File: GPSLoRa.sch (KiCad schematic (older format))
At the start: 31 parts, among them P1 IN EXT, P2 - INPUT 12 +, P3 OUT EXT, P4 Battery, Q1 Q_NPN_BCE, U1 4N26, U2 LM2596_Breakout, U3 4N26, U4 RFM95W-868S2, U5 MCP73831T-2ATI/OT

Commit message: ChangeName LoRaCatTrack
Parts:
- A1: footprint (none) -> TIH:GSG-SMA-EDGE
- C1, C2, C3, D1: footprint (none) -> Capacitors_SMD:C_0805_HandSoldering
- D2: footprint (none) -> Diodes_ThroughHole:Diode_TO-220_Horizontal_LargePads
- D3: footprint (none) -> Diodes_ThroughHole:Diode_DO-41_SOD81_Horizontal_RM10
- D4, D5: footprint (none) -> LEDs:LED_0805
- MODULE1: footprint QUECTEL_L80-M39 -> TIH:QUECTEL_L80-M39
- P1, P3: footprint (none) -> Pin_Headers:Pin_Header_Straight_1x01
- P2, P4: footprint (none) -> Pin_Headers:Pin_Header_Straight_1x02
- R1, R2, R3, R4, R5, R6, R7, R8, R9: footprint (none) -> Resistors_SMD:R_0805_HandSoldering
- U1, U3: footprint DIP-6 -> Housings_DIP:DIP-6_W7.62mm_LongPads
- U4: footprint XCVR_RFM95W-868S2 -> TIH:XCVR_RFM95W-868S2
- U5: footprint SOT95P300X145-5N -> TO_SOT_Packages_SMD:SOT-23-5

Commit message: Added PCB
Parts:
- added D6: POWER, LEDs:LED_0805, symbol LED
- added R10: R, Resistors_SMD:R_0805_HandSoldering, symbol R
- D1: footprint Capacitors_SMD:C_0805_HandSoldering -> Diodes_ThroughHole:Diode_DO-35_SOD27_Horizontal_RM10
- D2: footprint Diodes_ThroughHole:Diode_TO-220_Horizontal_LargePads -> Diodes_ThroughHole:Diode_DO-35_SOD27_Horizontal_RM10
- D3: footprint Diodes_ThroughHole:Diode_DO-41_SOD81_Horizontal_RM10 -> Diodes_ThroughHole:Diode_DO-35_SOD27_Horizontal_RM10
- JP1: footprint (none) -> Pin_Headers:Pin_Header_Straight_1x02
- Q1: footprint (none) -> TO_SOT_Packages_THT:TO-92_Inline_Narrow_Oval
- U2: footprint (none) -> TIH:LM2596DC-DC
- uP1: footprint (none) -> TIH:arduinoMiniPro2
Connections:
- net +BATT: now also R10.1
- net GND: now also D6.1 (K)
- new net: D6.2 (A), R10.2
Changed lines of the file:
@@
 F 0 "uP1" H 2350 -250 60  0000 C CNN
 F 1 "ARDUPROMINI" H 1800 -200 60  0000 C CNN
-F 2 "" H 2850 650 60  0001 C CNN
+F 2 "TIH:arduinoMiniPro2" H 2850 650 60  0001 C CNN
 F 3 "" H 2850 650 60  0000 C CNN
 	1    2850 650
@@
 F 0 "JP1" H 5100 4700 50  0000 C CNN
 F 1 "JUMPER" H 5100 4470 50  0000 C CNN
-F 2 "" H 5100 4550 50  0001 C CNN
+F 2 "Pin_Headers:Pin_Header_Straight_1x02" H 5100 4550 50  0001 C CNN
 F 3 "" H 5100 4550 50  0000 C CNN
 	1    5100 4550
@@
 F 0 "D2" H 2350 4700 50  0000 C CNN
 F 1 "1N4007" H 2350 4500 50  0000 C CNN
-F 2 "Diodes_ThroughHole:Diode_TO-220_Horizontal_LargePads" H 2350 4600 50  0001 C CNN
+F 2 "Diodes_ThroughHole:Diode_DO-35_SOD27_Horizontal_RM10" H 2350 4600 50  0001 C CNN
 F 3 "" H 2350 4600 50  0000 C CNN
 	1    2350 4600
@@
 F 0 "Q1" H 5585 5935 50  0000 R CNN
 F 1 "Q_NPN_BCE" H 5885 5835 50  0000 R CNN
-F 2 "" H 5485 5985 50  0001 C CNN
+F 2 "TO_SOT_Packages_THT:TO-92_Inline_Narrow_Oval" H 5485 5985 50  0001 C CNN
 F 3 "" H 5285 5885 50  0000 C CNN
 	1    5285 5885
@@
 F 0 "D1" H 1455 6370 50  0000 C CNN
 F 1 "D" H 1455 6170 50  0000 C CNN
-F 2 "Capacitors_SMD:C_0805_HandSoldering" H 1455 6270 50  0001 C CNN
+F 2 "Diodes_ThroughHole:Diode_DO-35_SOD27_Horizontal_RM10" H 1455 6270 50  0001 C CNN
 F 3 "" H 1455 6270 50  0000 C CNN
 	1    1455 6270
@@
 F 0 "D3" H 5385 5505 50  0000 C CNN
 F 1 "D" H 5385 5305 50  0000 C CNN
-F 2 "Diodes_ThroughHole:Diode_DO-41_SOD81_Horizontal_RM10" H 5385 5405 50  0001 C CNN
+F 2 "Diodes_ThroughHole:Diode_DO-35_SOD27_Horizontal_RM10" H 5385 5405 50  0001 C CNN
 F 3 "" H 5385 5405 50  0000 C CNN
 	1    5385 5405
@@
 F 0 "U2" H 2900 5000 60  0000 C CNN
 F 1 "LM2596_Breakout" H 3550 4400 60  0000 C CNN
-F 2 "" H 3400 4700 60  0001 C CNN
+F 2 "TIH:LM2596DC-DC" H 3400 4700 60  0001 C CNN
 F 3 "" H 3400 4700 60  0000 C CNN
 	1    3400 4700
@@
 	1    0    0    -1
 $EndComp
+$Comp
+L LED D6
+U 1 1 583891C8
+P 4235 3370
+F 0 "D6" H 4235 3470 50  0000 C CNN
+F 1 "POWER" H 4235 3270 50  0000 C CNN
+F 2 "LEDs:LED_0805" H 4235 3370 50  0001 C CNN
+F 3 "" H 4235 3370 50  0000 C CNN
+	1    4235 3370
+	1    0    0    -1
+$EndComp
+$Comp
+L R R10
+U 1 1 583892C7
+P 4715 3370
+F 0 "R10" V 4795 3370 50  0000 C CNN
+F 1 "R" V 4715 3370 50  0000 C CNN
+F 2 "Resistors_SMD:R_0805_HandSoldering" V 4645 3370 50  0001 C CNN
+F 3 "" H 4715 3370 50  0000 C CNN
+	1    4715 3370
+	0    1    1    0
+$EndComp
+Wire Wire Line
+	4565 3370 4435 3370
+$Comp
+L GND #PWR027
+U 1 1 58389C04
+P 3810 3485
+F 0 "#PWR027" H 3810 3235 50  0001 C CNN
+F 1 "GND" H 3810 3335 50  0000 C CNN
+F 2 "" H 3810 3485 50  0000 C CNN
+F 3 "" H 3810 3485 50  0000 C CNN
+	1    3810 3485
+	1    0    0    -1
+$EndComp
+Wire Wire Line
+	3810 3485 3810 3370
+Wire Wire Line
+	3810 3370 4035 3370
+Wire Wire Line
+	4975 3270 4975 3370
+Wire Wire Line
+	4975 3370 4865 3370
+$Comp
+L +BATT #PWR028
+U 1 1 5838A13A
+P 4975 3270
+F 0 "#PWR028" H 4975 3120 50  0001 C CNN
+F 1 "+BATT" H 4975 3410 50  0000 C CNN
+F 2 "" H 4975 3270 50  0000 C CNN
+F 3 "" H 4975 3270 50  0000 C CNN
+	1    4975 3270
+	1    0    0    -1
+$EndComp

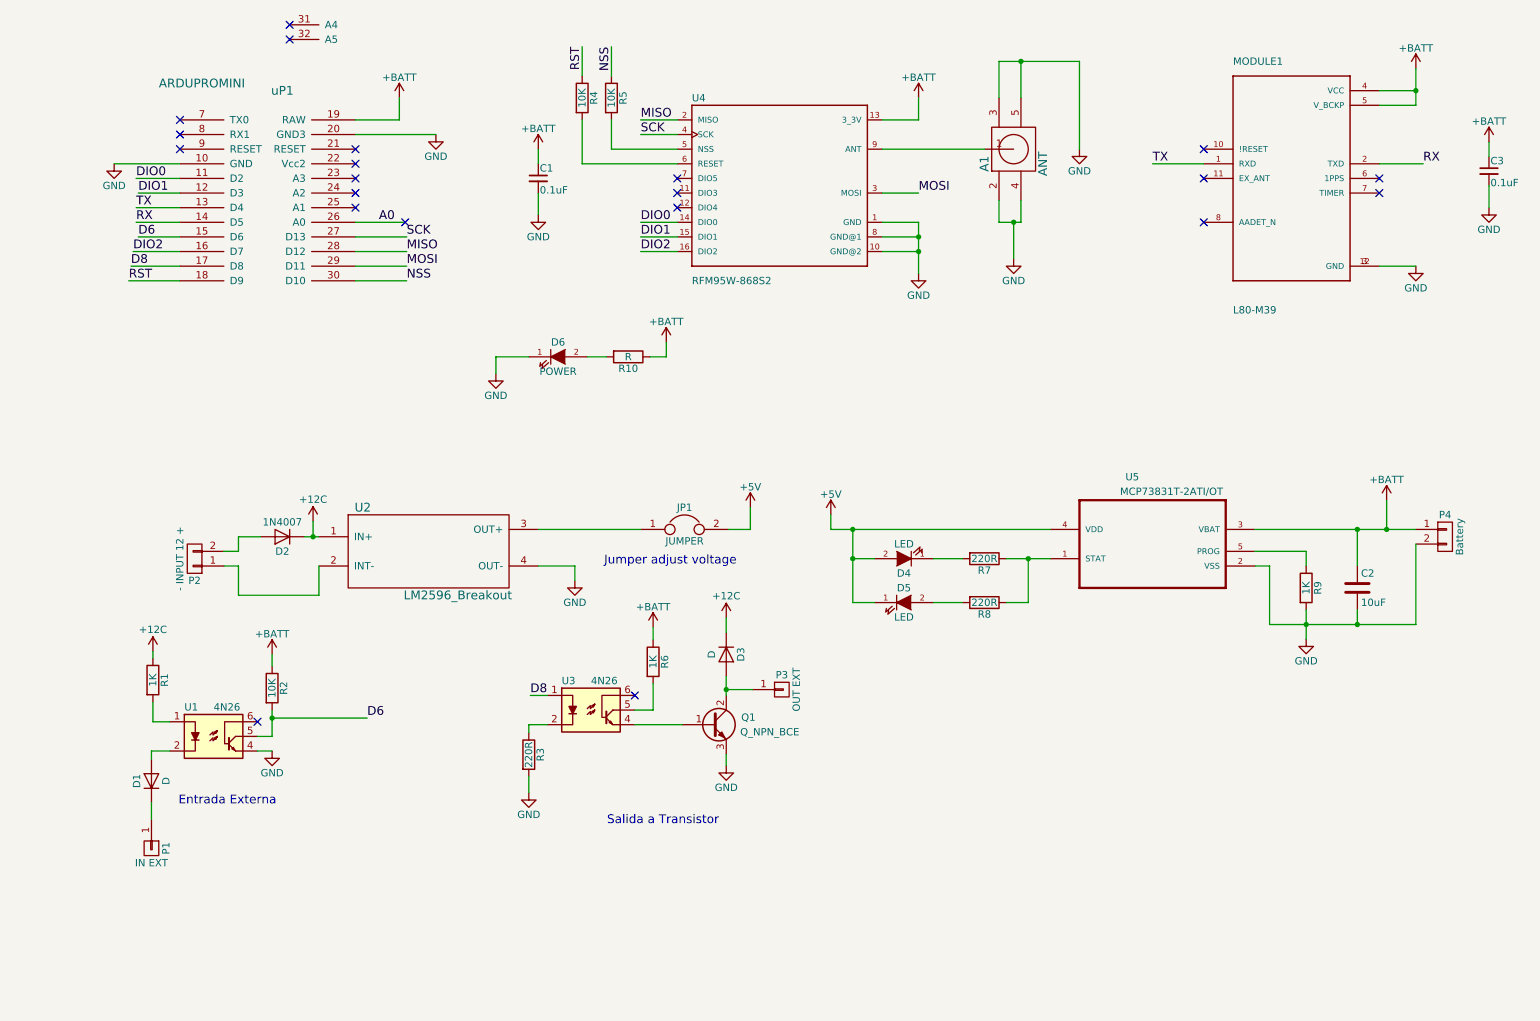
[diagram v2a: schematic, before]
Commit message: Update v0.3_beta
Added  button, added in external
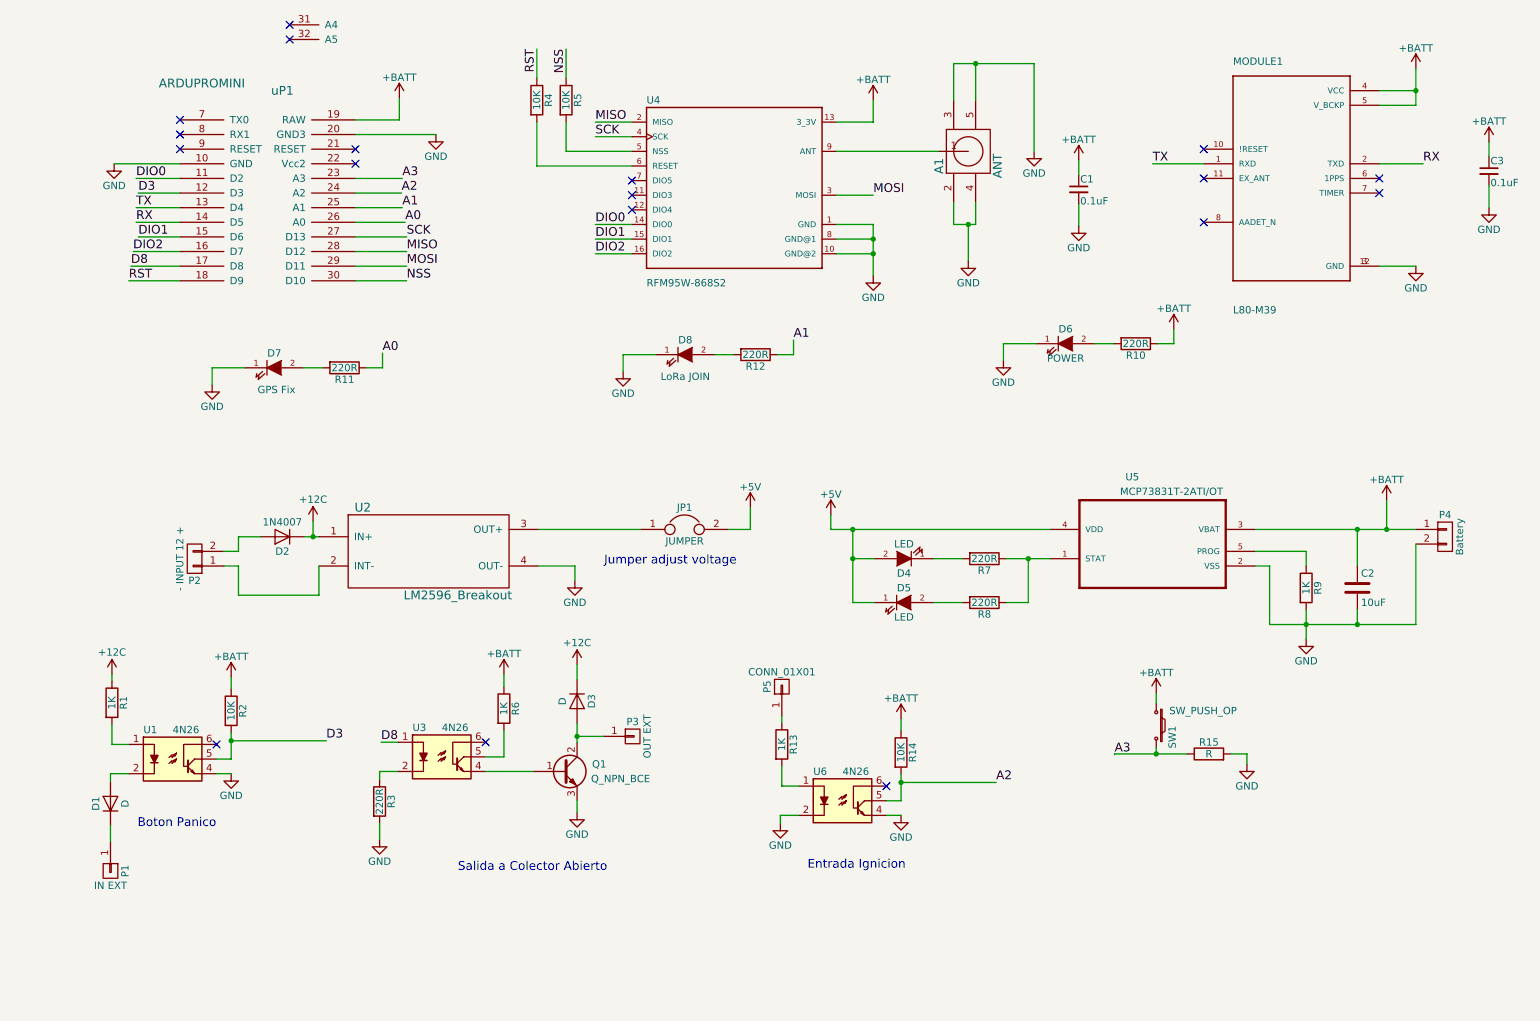
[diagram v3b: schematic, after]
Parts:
- added D7: GPS Fix, LEDs:LED_0805, symbol LED
- added D8: LoRa JOIN, LEDs:LED_0805, symbol LED
- added P5: CONN_01X01, symbol CONN_01X01
- added R11, R12: 220R, Resistors_SMD:R_0805_HandSoldering, symbol R
- added R13: 1K, Resistors_SMD:R_0805_HandSoldering, symbol R
- added R14: 10K, Resistors_SMD:R_0805_HandSoldering, symbol R
- added R15: R, symbol R
- added SW1: SW_PUSH_OP, symbol SW_PUSH_SMALL_H
- added U6: 4N26, Housings_DIP:DIP-6_W7.62mm_LongPads, symbol 4N26
- R10: value R -> 220R
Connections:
- net +BATT: now also R14.1, SW1.1
- net A0: now also R11.1
- net DIO1: now also uP1.15 (D6); no longer uP1.12 (D3)
- net GND: now also D7.1 (K), D8.1 (K), R15.2, U6.2, U6.4
- net A3: now reaches uP1.23 (A3)
- net A3: now also R15.1, SW1.2
- net A2: now reaches uP1.24 (A2)
- net A2: now also R14.2, U6.5
- net A1: now reaches uP1.25 (A1)
- net A1: now also R12.1
- net D6 renamed D3
- net D3: now also uP1.12 (D3); no longer uP1.15 (D6)
- new net: D7.2 (A), R11.2
- new net: D8.2 (A), R12.2
- new net: R13.2, U6.1
- new net: P5.1 (P1), R13.1
- no-connect marks 21 -> 18
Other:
- note added: "Boton Panico"
- note added: "Entrada Ignicion"
- note added: "Salida a Colector Abierto"
- note removed: "Entrada Externa"
- note removed: "Salida a Transistor"
- moved on the sheet: A1, C1, D1, D3, D6, P1, P3, Q1, R1, R10, R2, R3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

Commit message: Added regulator 3.3v
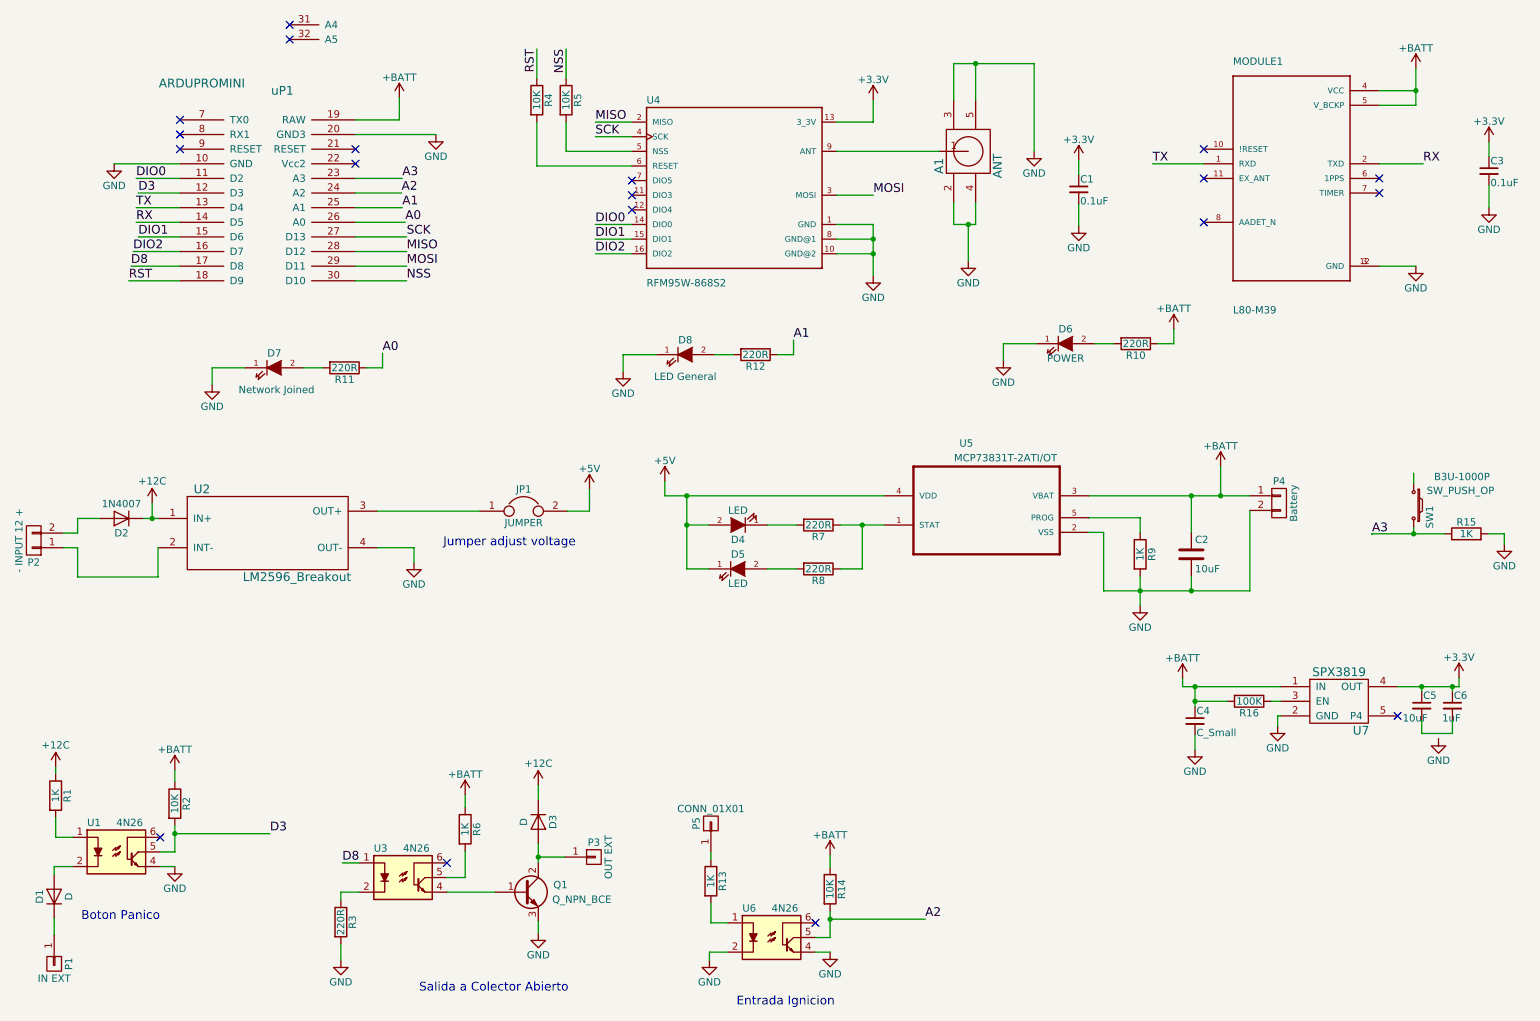
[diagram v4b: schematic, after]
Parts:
- added C4: C_Small, Capacitors_SMD:C_0805_HandSoldering, symbol C_Small
- added C5: 10uF, Capacitors_SMD:C_0805_HandSoldering, symbol C_Small
- added C6: 1uF, Capacitors_SMD:C_0805_HandSoldering, symbol C_Small
- added R16: 100K, Resistors_SMD:R_0805_HandSoldering, symbol R
- added U7: SPX3819, TO_SOT_Packages_SMD:SOT-23-5, symbol SPX3819
- D7: value GPS Fix -> Network Joined
- D8: value LoRa JOIN -> LED General
- P5: footprint (none) -> Socket_Strips:Socket_Strip_Straight_1x01
- R15: value R -> 1K; footprint (none) -> Resistors_SMD:R_0805_HandSoldering
- SW1: footprint (none) -> TIH:SW_B3U-1000P
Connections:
- net +BATT: now also C4.1, R16.2, U7.1 (IN); no longer C1.1, C3.1, SW1.1, U4.13 (3_3V)
- net GND: now also C4.2, U7.2 (GND)
- new net: R16.1, U7.3 (EN)
- new net: C5.2, C6.2
- new net +3V3: C1.1, C3.1, C5.1, C6.1, U4.13 (3_3V), U7.4 (OUT)
- no-connect marks 18 -> 19
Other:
- moved on the sheet: C2, D1, D2, D3, D4, D5, JP1, P1, P2, P3, P4, P5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

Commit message: Correct Pullup
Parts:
- C4: value C_Small -> 0.1uF
- C5: value 10uF -> 22uF
- C6: value 1uF -> 0.1uF
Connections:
- net +3V3: now also MODULE1.4 (VCC), MODULE1.5 (V_BCKP), R15.2
- net +BATT: no longer MODULE1.4 (VCC), MODULE1.5 (V_BCKP)
- net GND: now also SW1.1; no longer R15.2
